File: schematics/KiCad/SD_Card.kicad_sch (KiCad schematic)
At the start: 13 parts, among them J6 Micro_SD_Card_Det_Hirose_DM3AT, U14 LP2950-3.3, U18 74HC4050

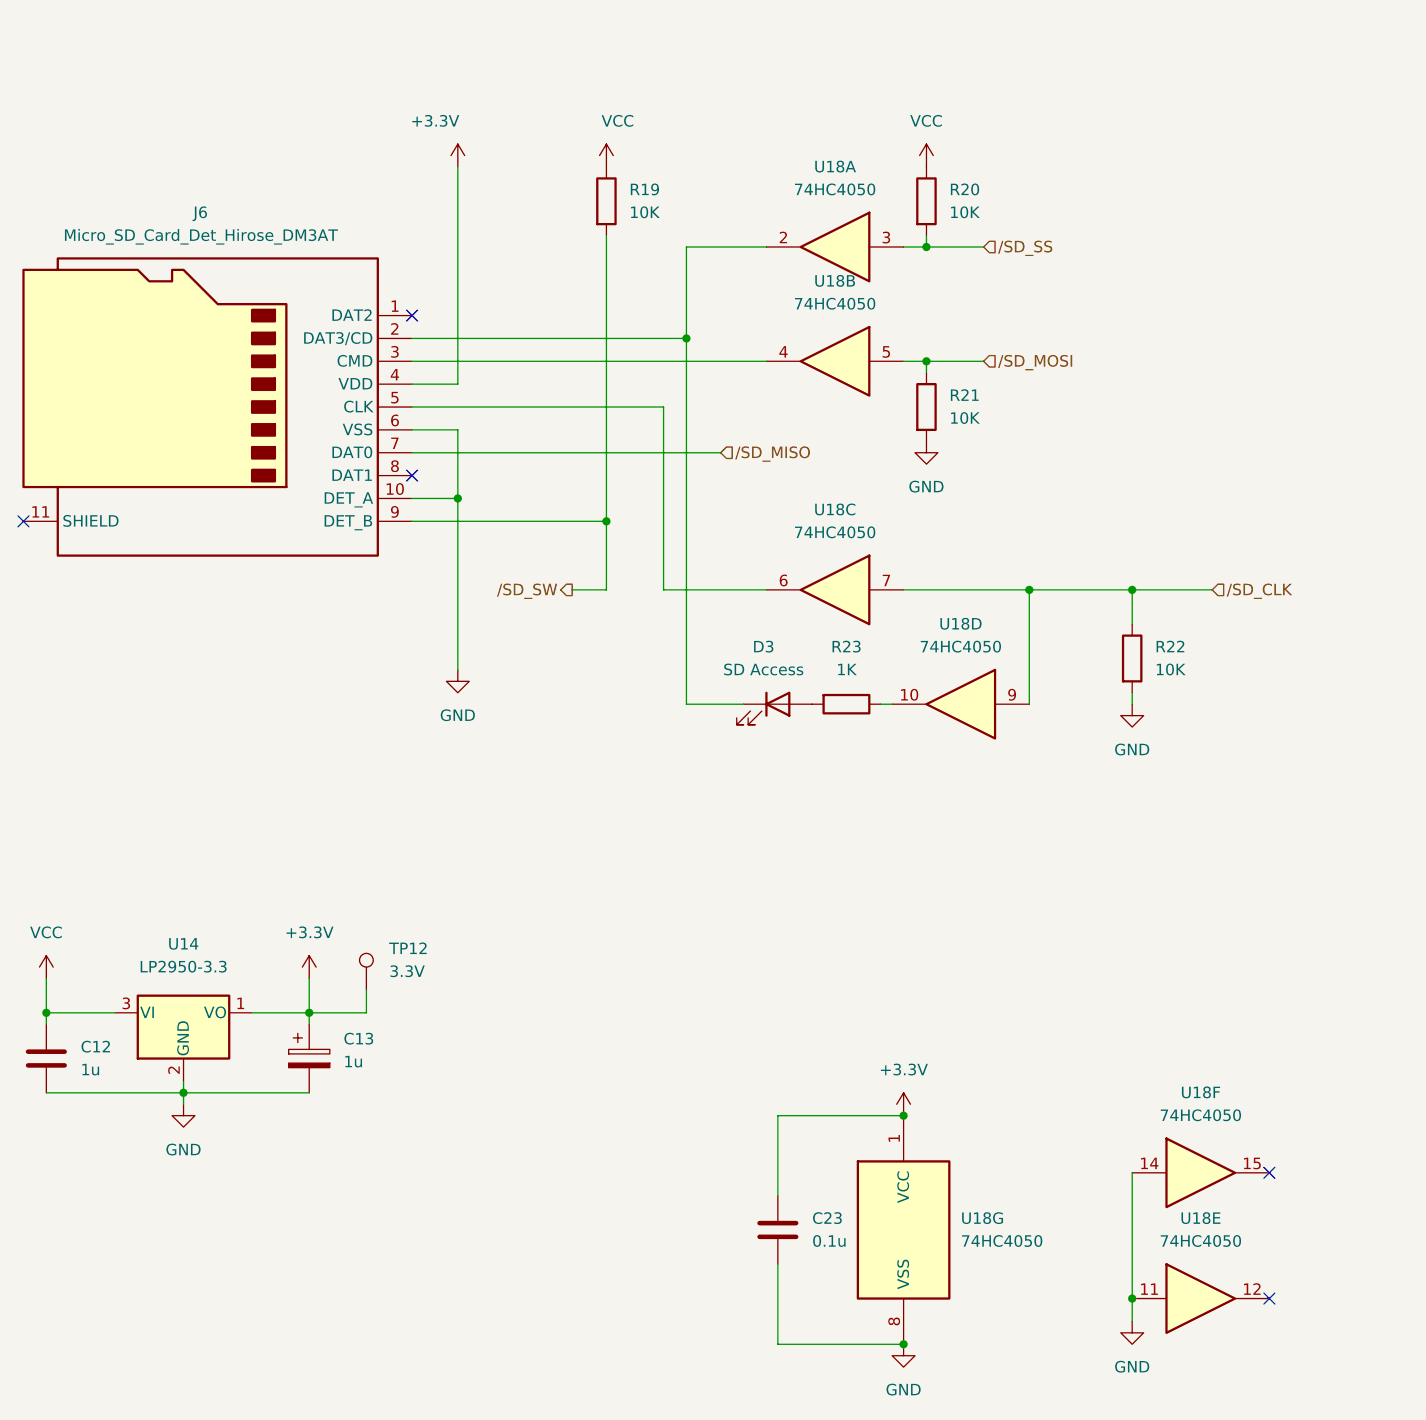
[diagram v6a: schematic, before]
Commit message: Define /WAIT_0 for IOREAD and INT
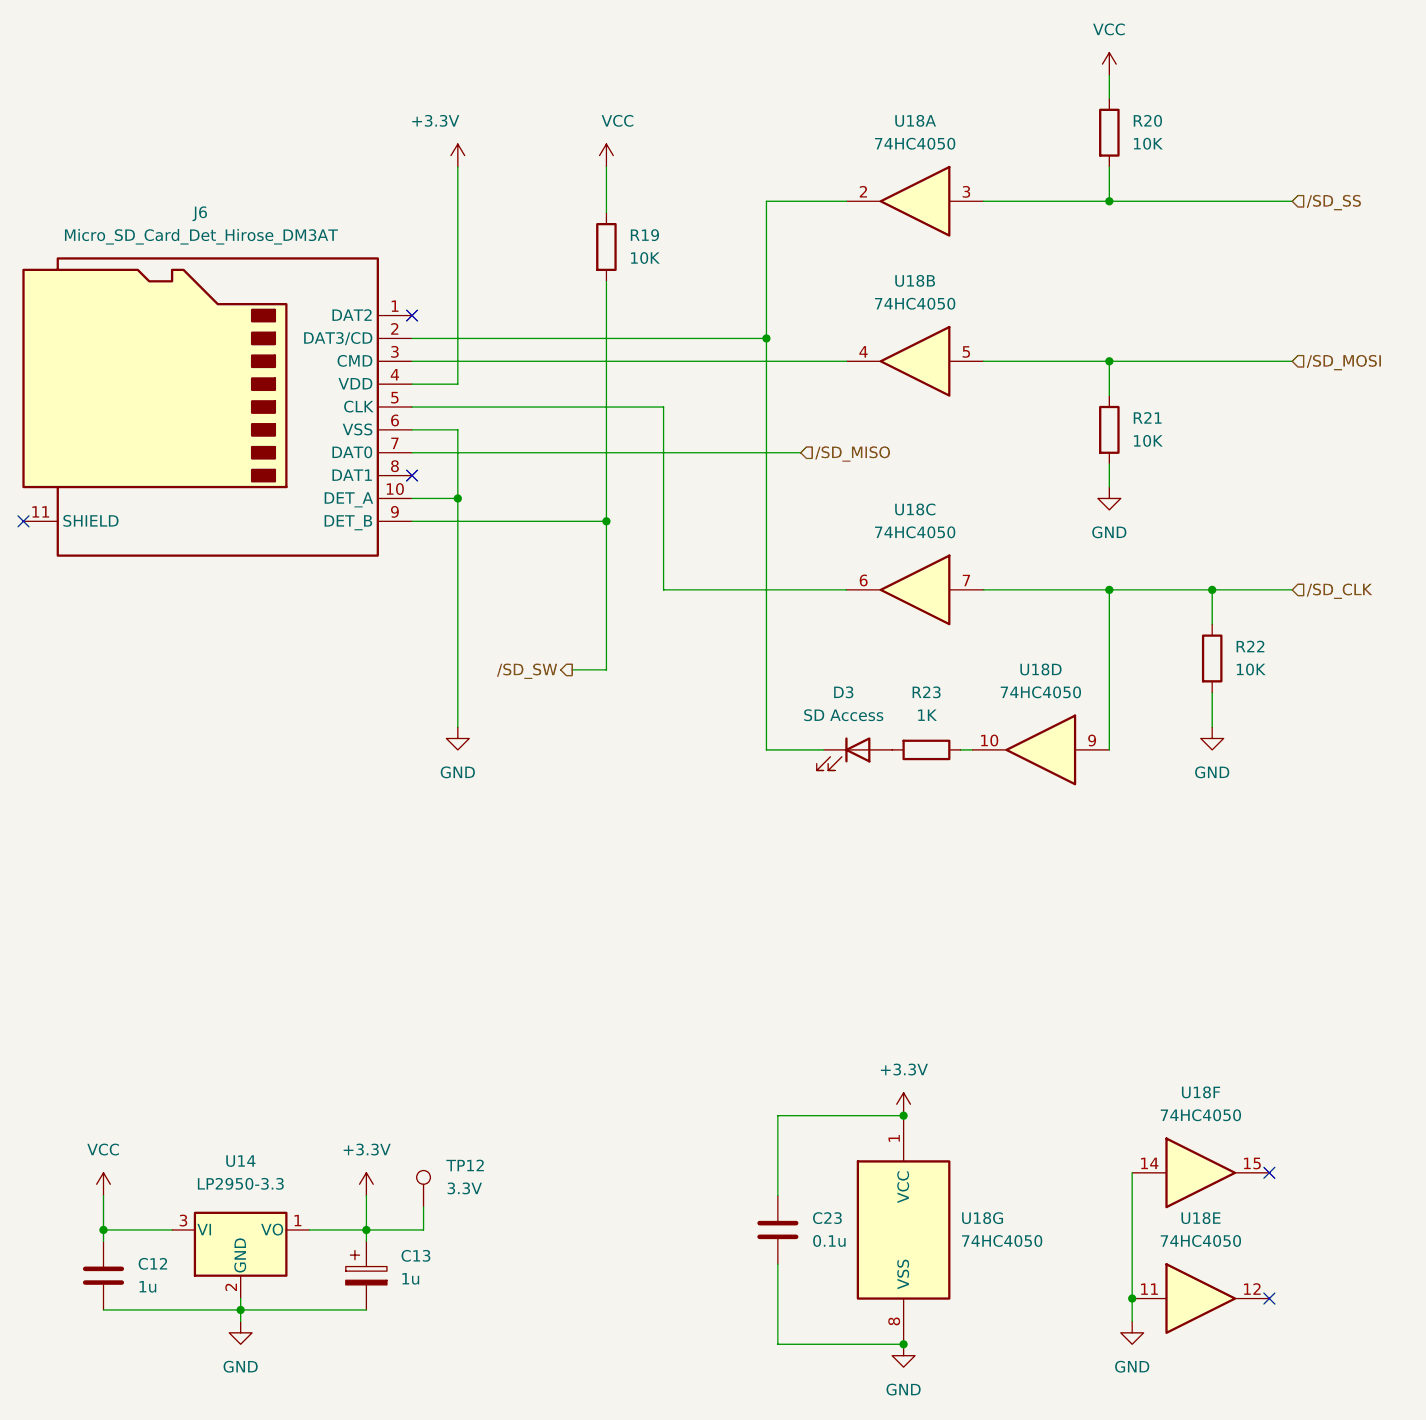
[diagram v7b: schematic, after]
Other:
- moved on the sheet: C12, C13, D3, R19, R20, R21, R22, R23, TP12, U14, U18A, U18B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

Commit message: Update schematics to support LED and DIP SW.
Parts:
- renumbered C23 to C21, D3 to D2, R20 to R18, R21 to R20, R22 to R21, R23 to R22, U18 to U16
